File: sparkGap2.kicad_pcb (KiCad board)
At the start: 4 copper layers, 52.7 x 54.1 mm, 45 parts, among them J1 9V, J2 IN, J3 OUT, Q1 BS170, SW2 pp, U1 TL072

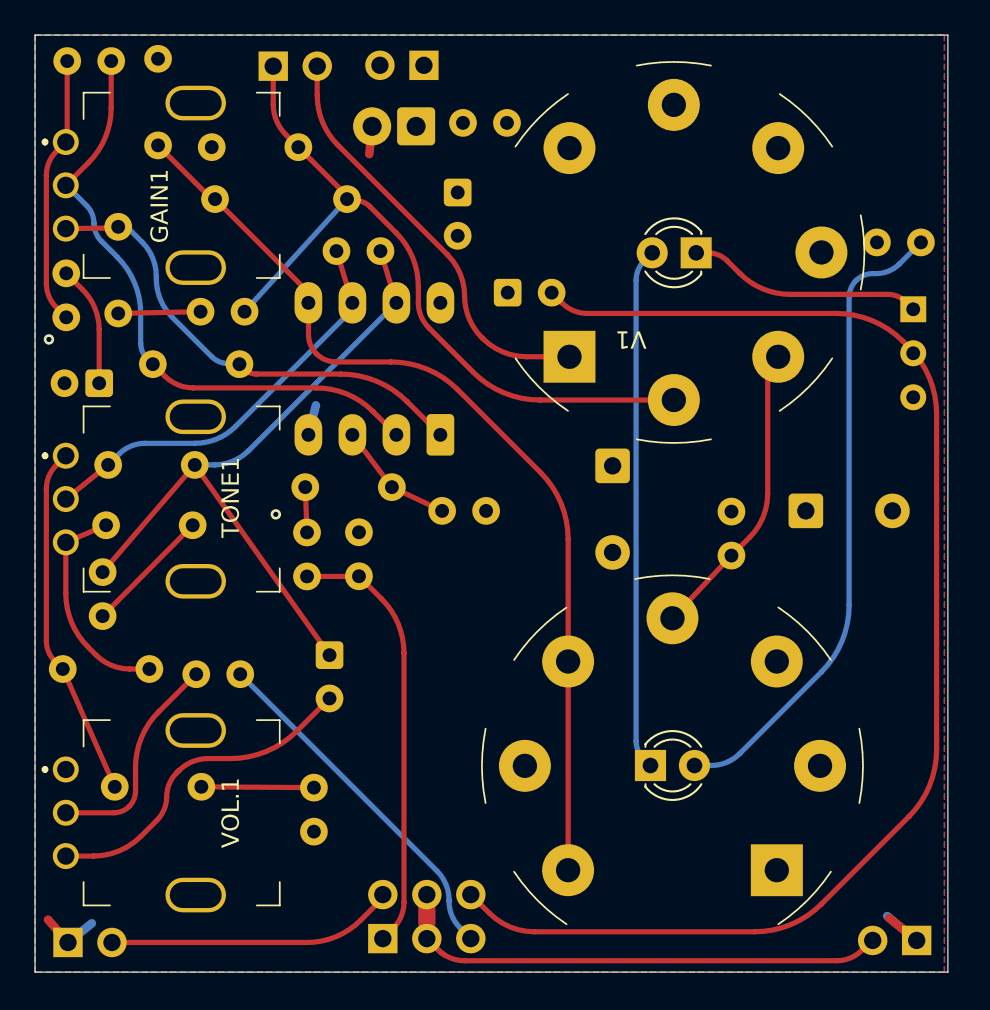
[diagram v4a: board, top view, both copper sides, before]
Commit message: Tweak PCB layout. Add enclosure drill template and GFX. Delete unused backups
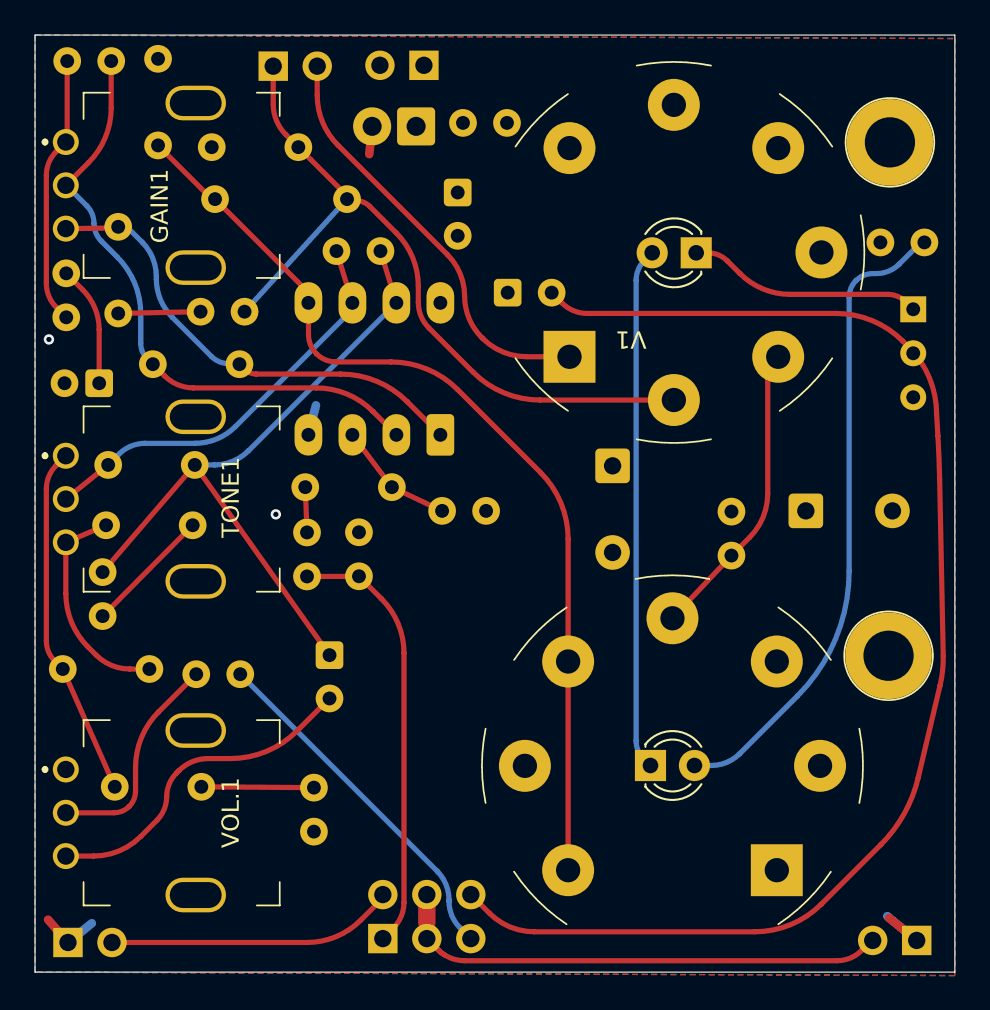
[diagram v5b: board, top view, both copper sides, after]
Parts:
- added board_mount_1: B9A-shield-single-mount, SamacSys_Parts:B9A-shield-single-mount, F.Cu at (150.9, 83.6)
- added board_mount_2: B9A-shield-single-mount, SamacSys_Parts:B9A-shield-single-mount, F.Cu at (150.8, 113.2)
- moved R14 0.20 mm to (165.3, 83.0)
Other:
- board size 52.7 x 54.1 mm -> 53.1 x 54.1 mm

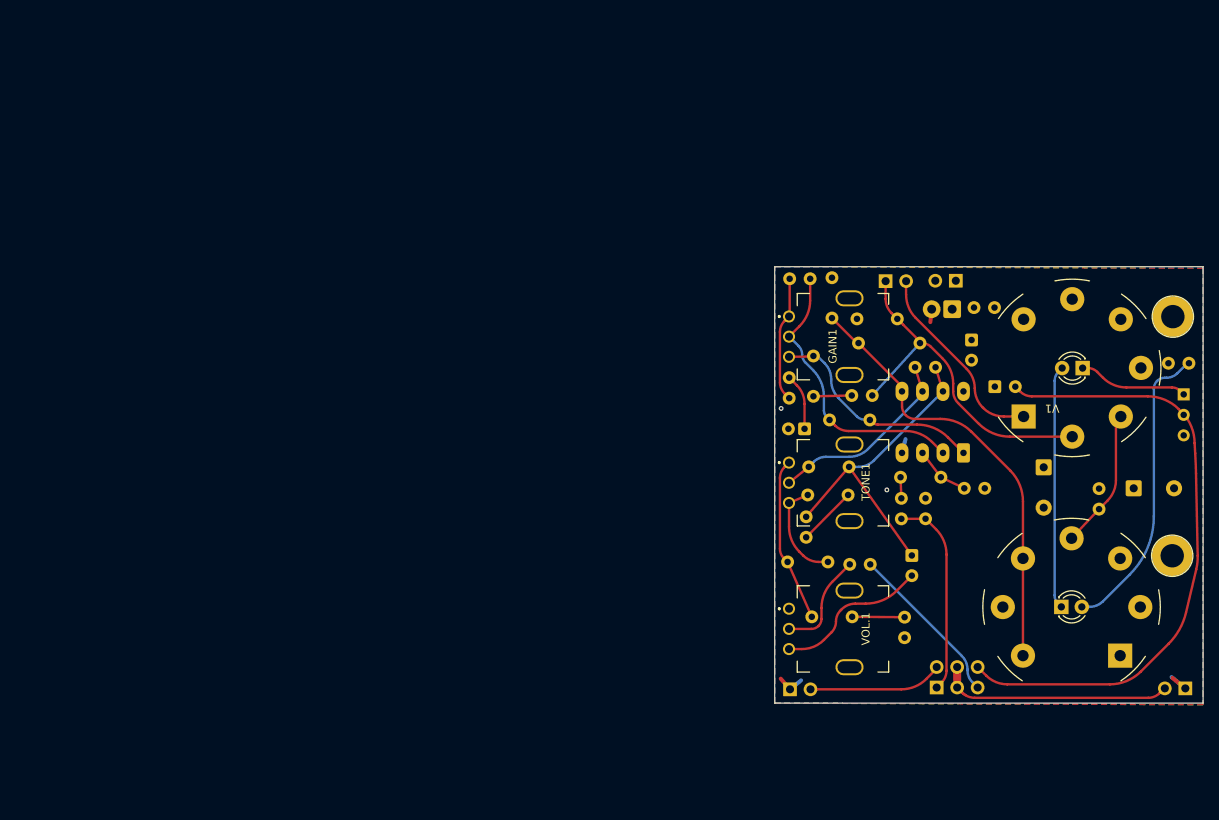
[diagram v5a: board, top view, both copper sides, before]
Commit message: move mount holes to 60 deg.
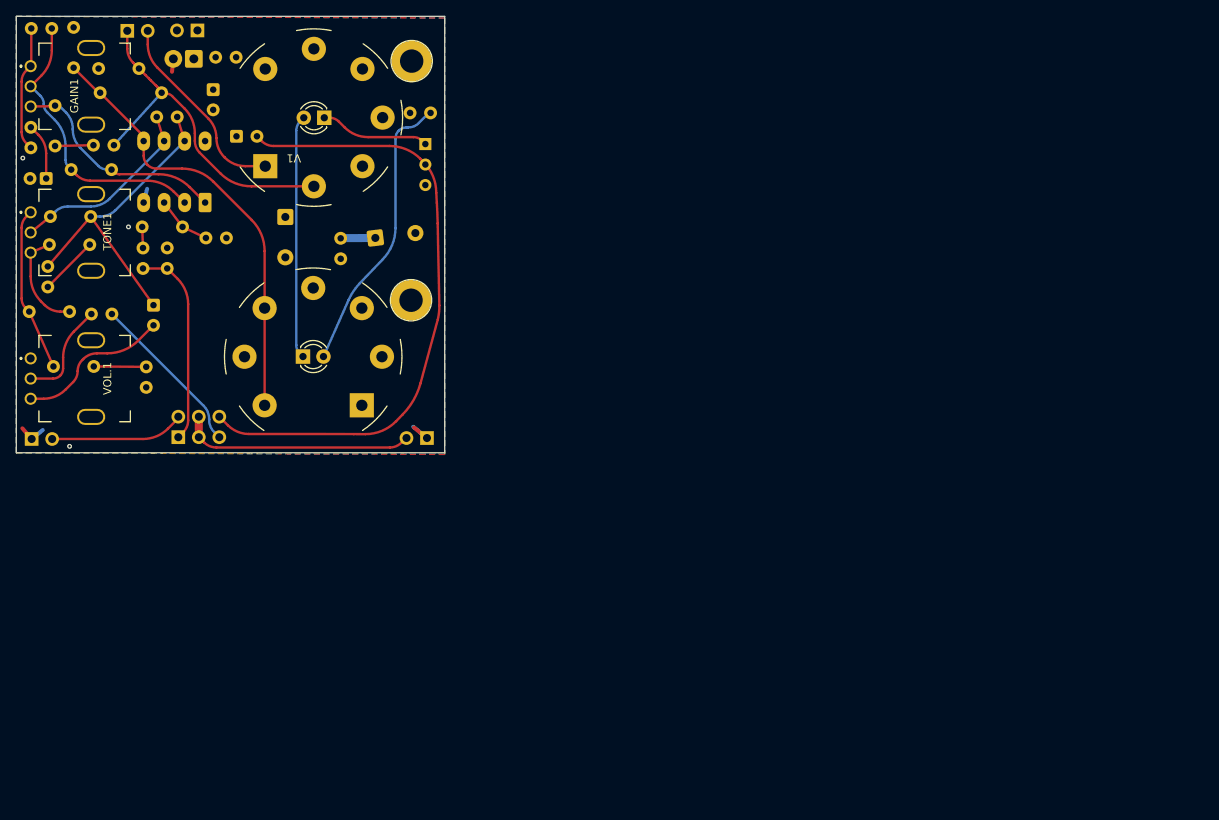
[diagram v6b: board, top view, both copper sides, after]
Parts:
- moved REF** 99.0 mm to (46.3, 77.2)
- moved V2 99.0 mm to (56.8, 82.2)
- moved board_mount_2 99.0 mm to (56.8, 82.2), turned to -60 degrees
- moved C1 99.0 mm to (53.3, 64.9)
- moved C10 99.0 mm to (29.2, 64.8)
- moved C11 99.0 mm to (29.1, 68.3)
- moved C12 99.0 mm to (24.6, 83.4)
- moved C13 99.0 mm to (37.0, 75.8)
- moved C14 99.0 mm to (26.6, 76.6)
- moved C2 99.0 mm to (40.6, 66.1)
- moved C3 99.0 mm to (64.5, 67.5), turned to 7 degrees
- moved C4 99.0 mm to (44.4, 49.1)
- moved C5 99.0 mm to (31.8, 59.0)
- moved C6 99.0 mm to (23.7, 60.1)
- moved C7 99.0 mm to (24.8, 51.1)
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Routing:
- net Net-(D3-A): track 36.8 -> 35.2 mm
- net Net-(D2-A): track 77.7 -> 78.4 mm
- net 4.5V: track 75.3 -> 75.9 mm
- net Earth: vias 2 -> 3

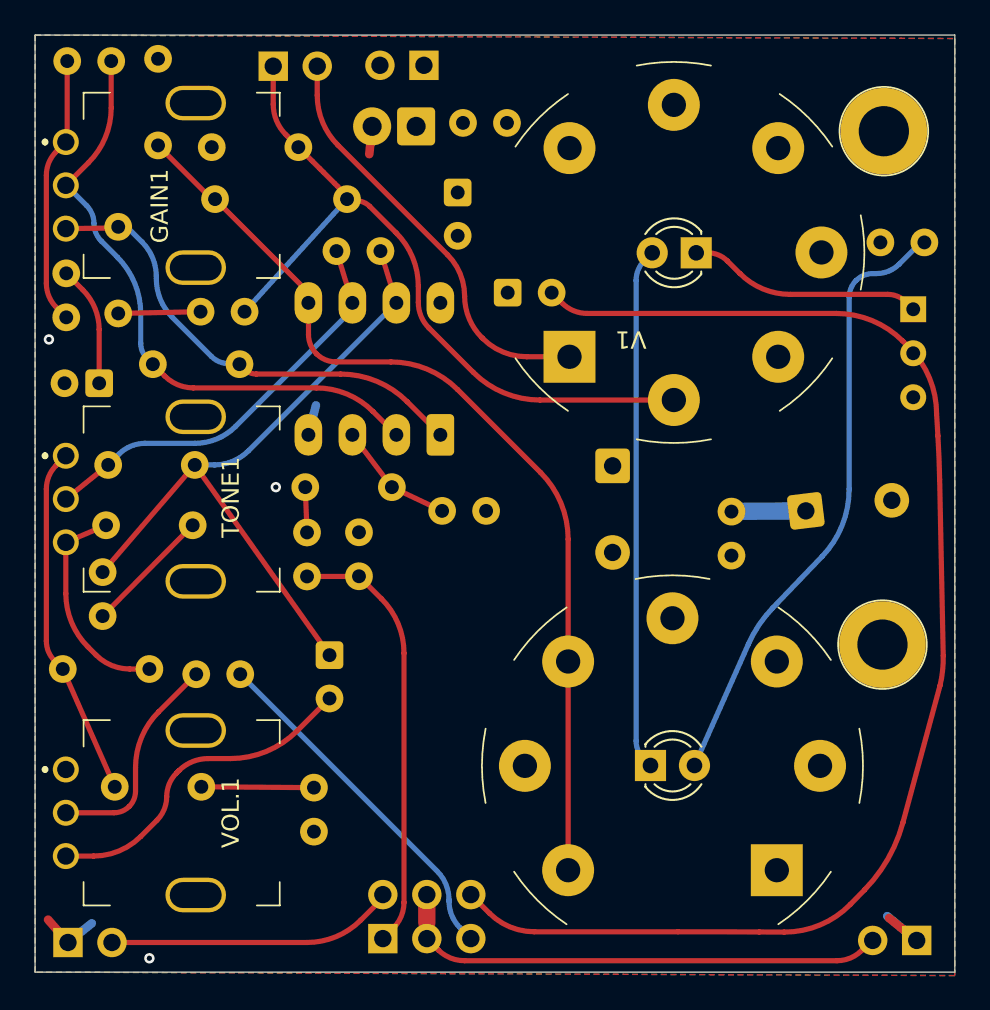
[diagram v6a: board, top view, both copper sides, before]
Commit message: Slight adjustments to layout. Clean up component numbering.
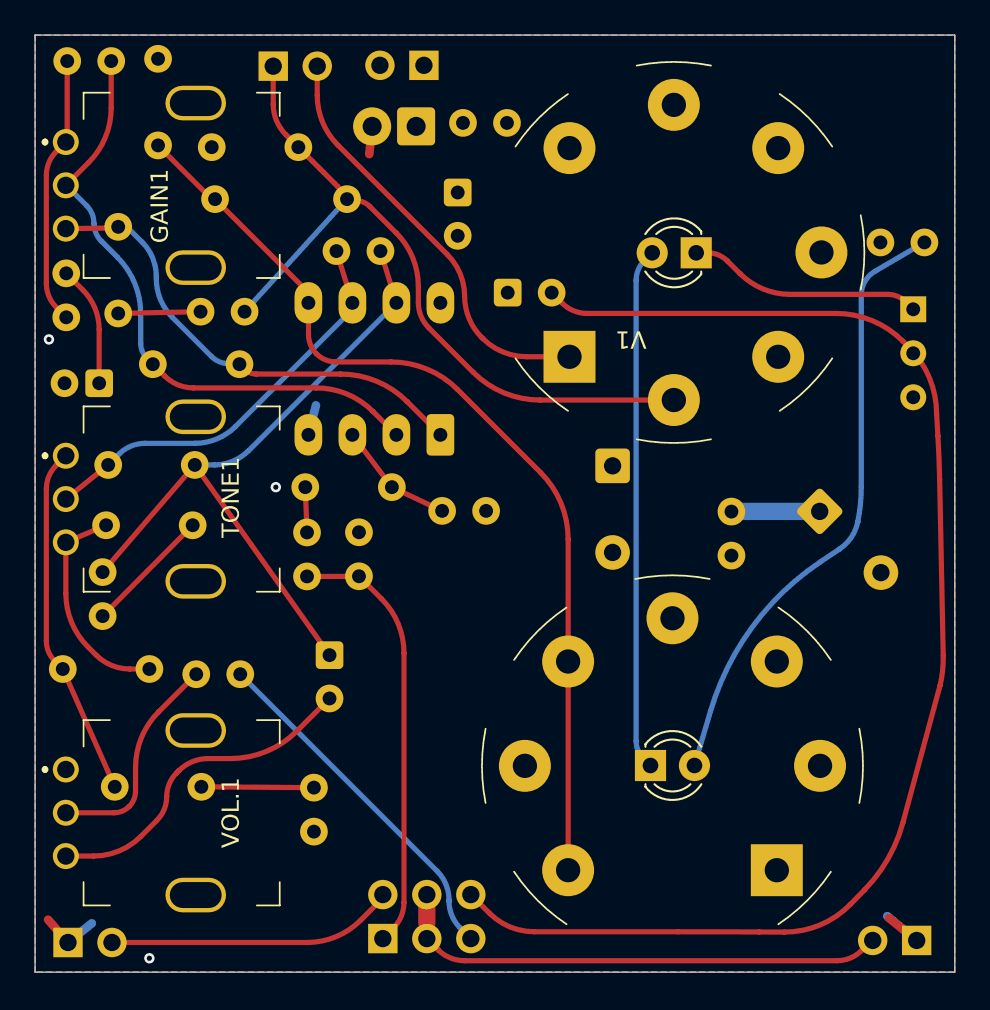
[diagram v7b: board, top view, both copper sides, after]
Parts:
- removed board_mount_1, board_mount_2: B9A-shield-single-mount, SamacSys_Parts:B9A-shield-single-mount
- moved C14 0.80 mm to (65.3, 67.5), turned to -45 degrees
- renumbered C2 to C1, C12 to C10, C13 to C11, C1 to C12, C4 to C13, C3 to C14, C5 to C2, C6 to C3, C7 to C4, C8 to C5, C9 to C6, C10 to C7, C11 to C8, C14 to C9, D3 to D2, D4 to D3, D2 to D4, R12 to R10, R13 to R11, R5 to R12, R3 to R13, R4 to R3, R6 to R4, R7 to R5, R8 to R6, R9 to R7, R10 to R8, R11 to R9, SW2 to SW1, SW1 to SW2
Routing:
- net 4.5V: track 75.9 -> 74.3 mm
- net 9V: track 17.3 -> 17.9 mm

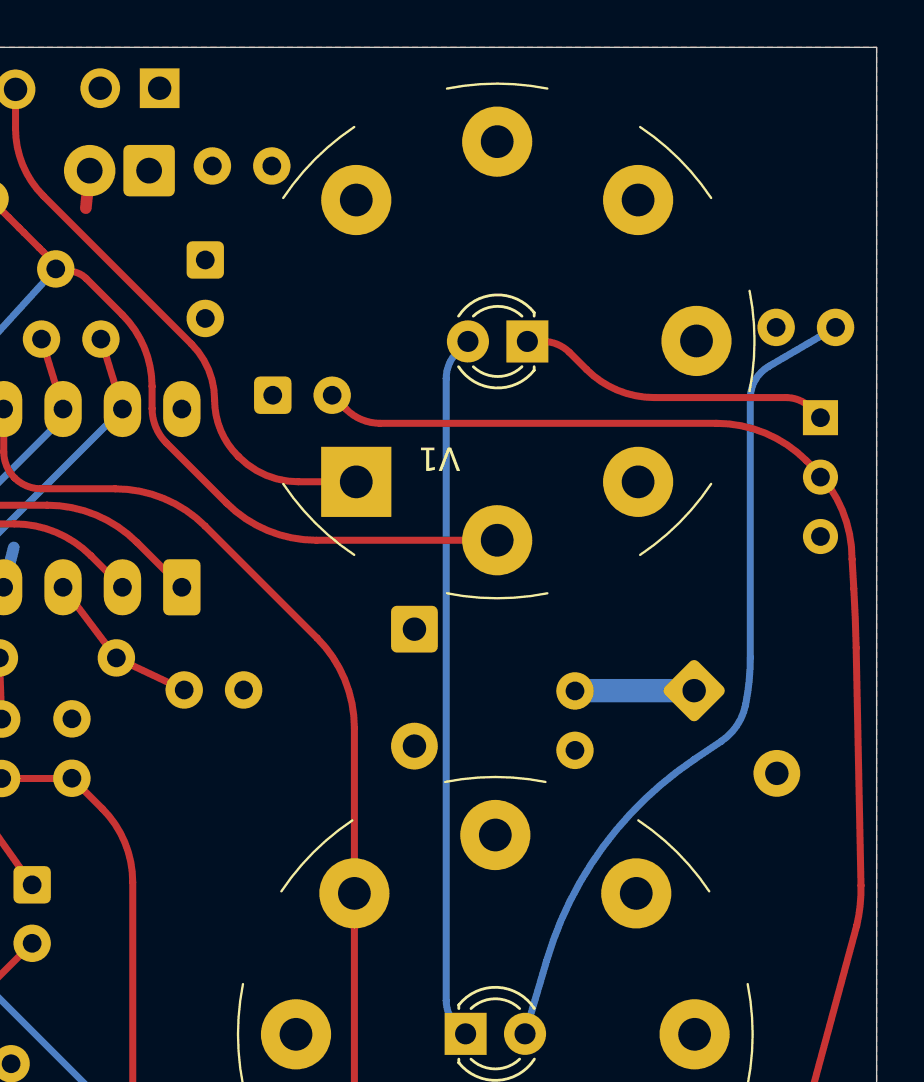
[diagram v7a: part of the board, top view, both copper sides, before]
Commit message: add back mount holes
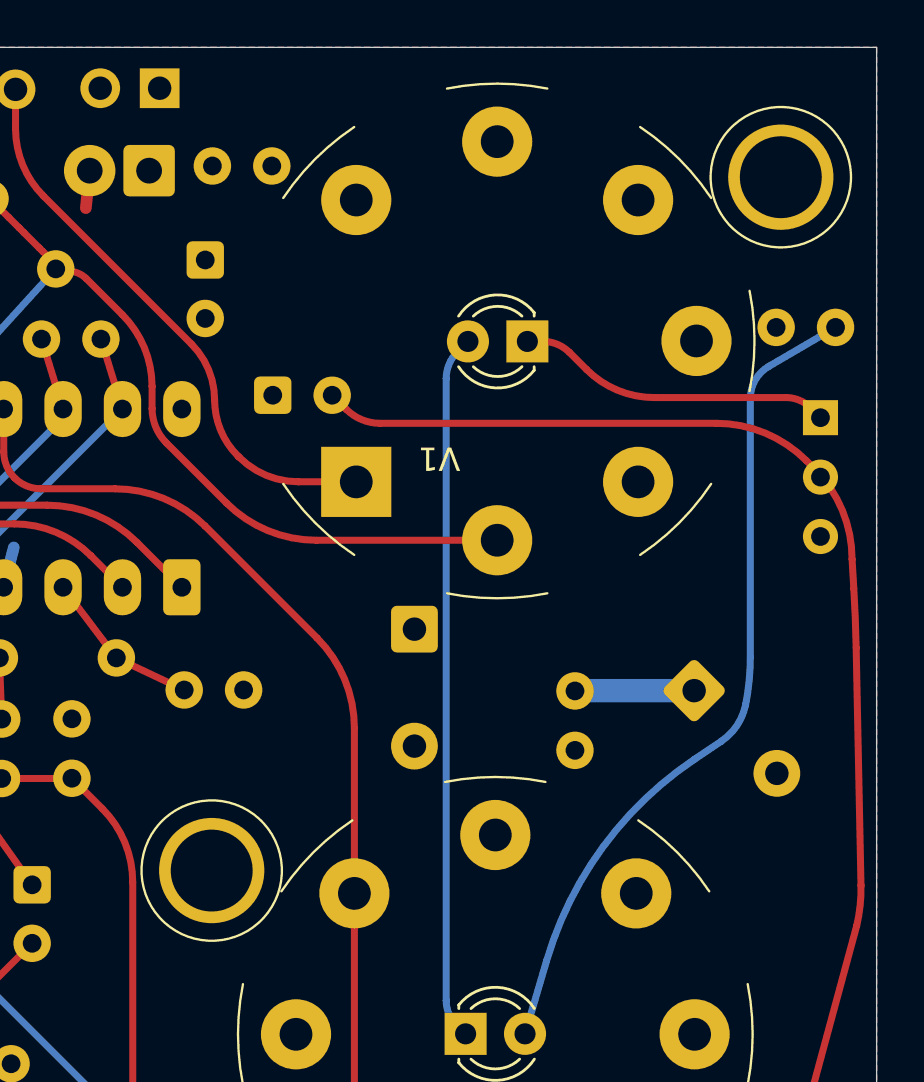
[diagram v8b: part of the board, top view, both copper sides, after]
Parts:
- added REF**: B9A-shield-single-mount, SamacSys_Parts:B9A-shield-single-mount, F.Cu at (56.8, 82.2)
- added REF**: B9A-shield-single-mount, SamacSys_Parts:B9A-shield-single-mount, F.Cu at (56.9, 52.5)
